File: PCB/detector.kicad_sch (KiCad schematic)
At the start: 17 parts, among them J6 Through, J8 Audio In, U2 TL072, U3 LM393

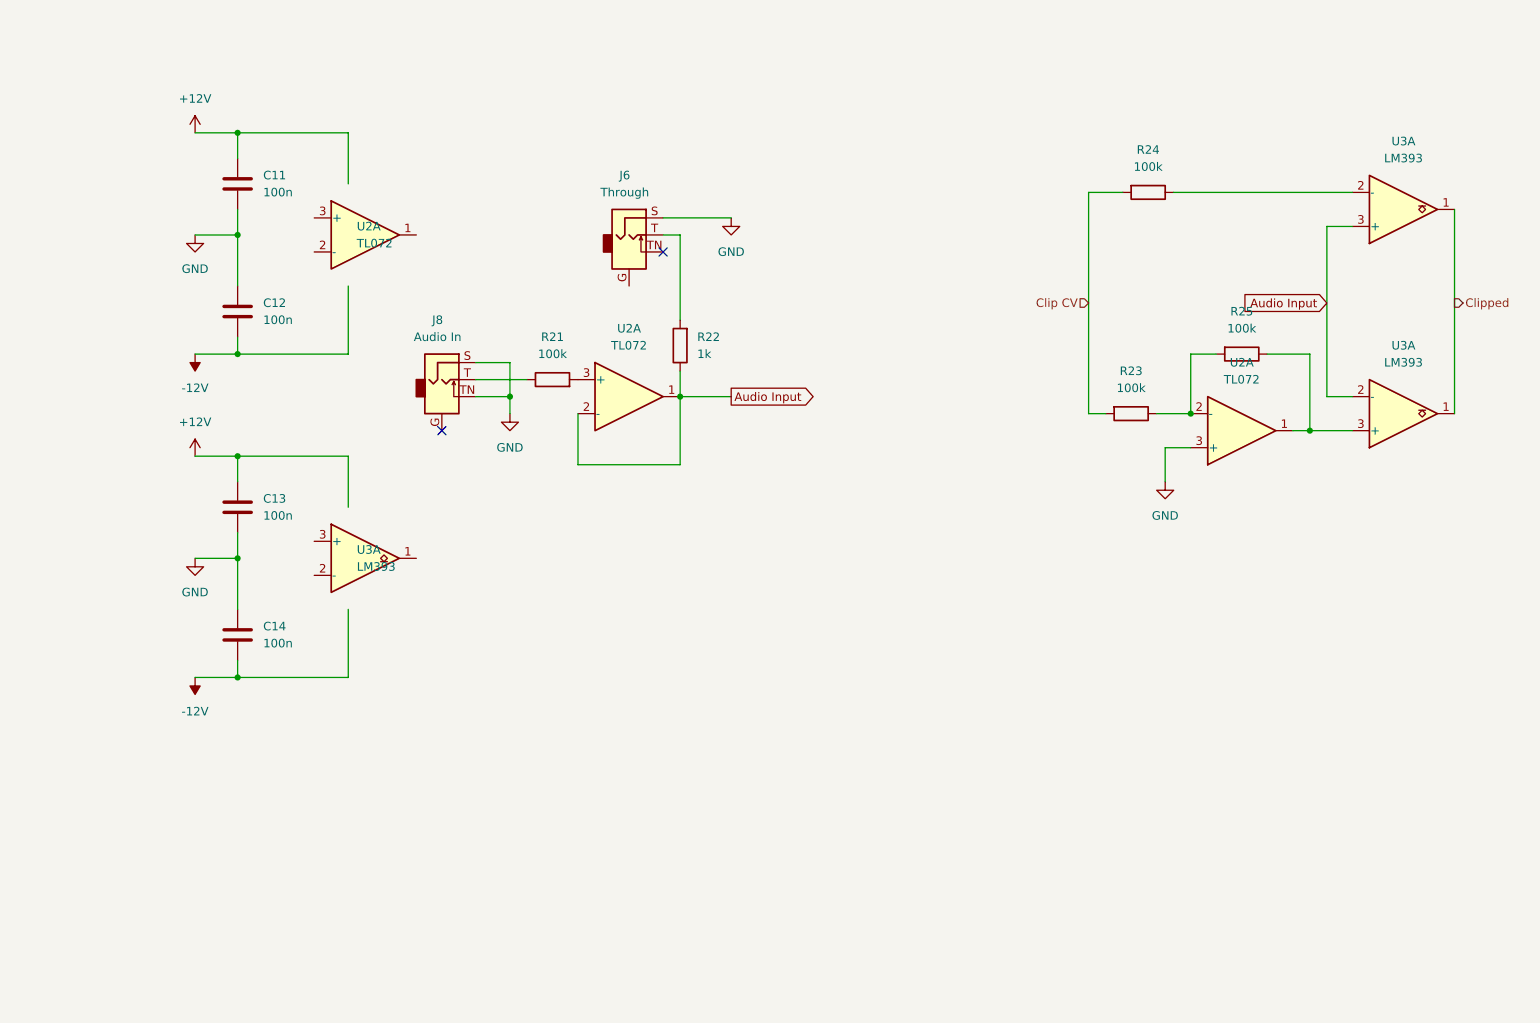
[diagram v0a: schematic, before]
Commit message: :art: Improve layout/positioning on main sheet
Also condense the voltage divider for the clip delay threshold,
as there is no load on this part and it can be shared between buffers.
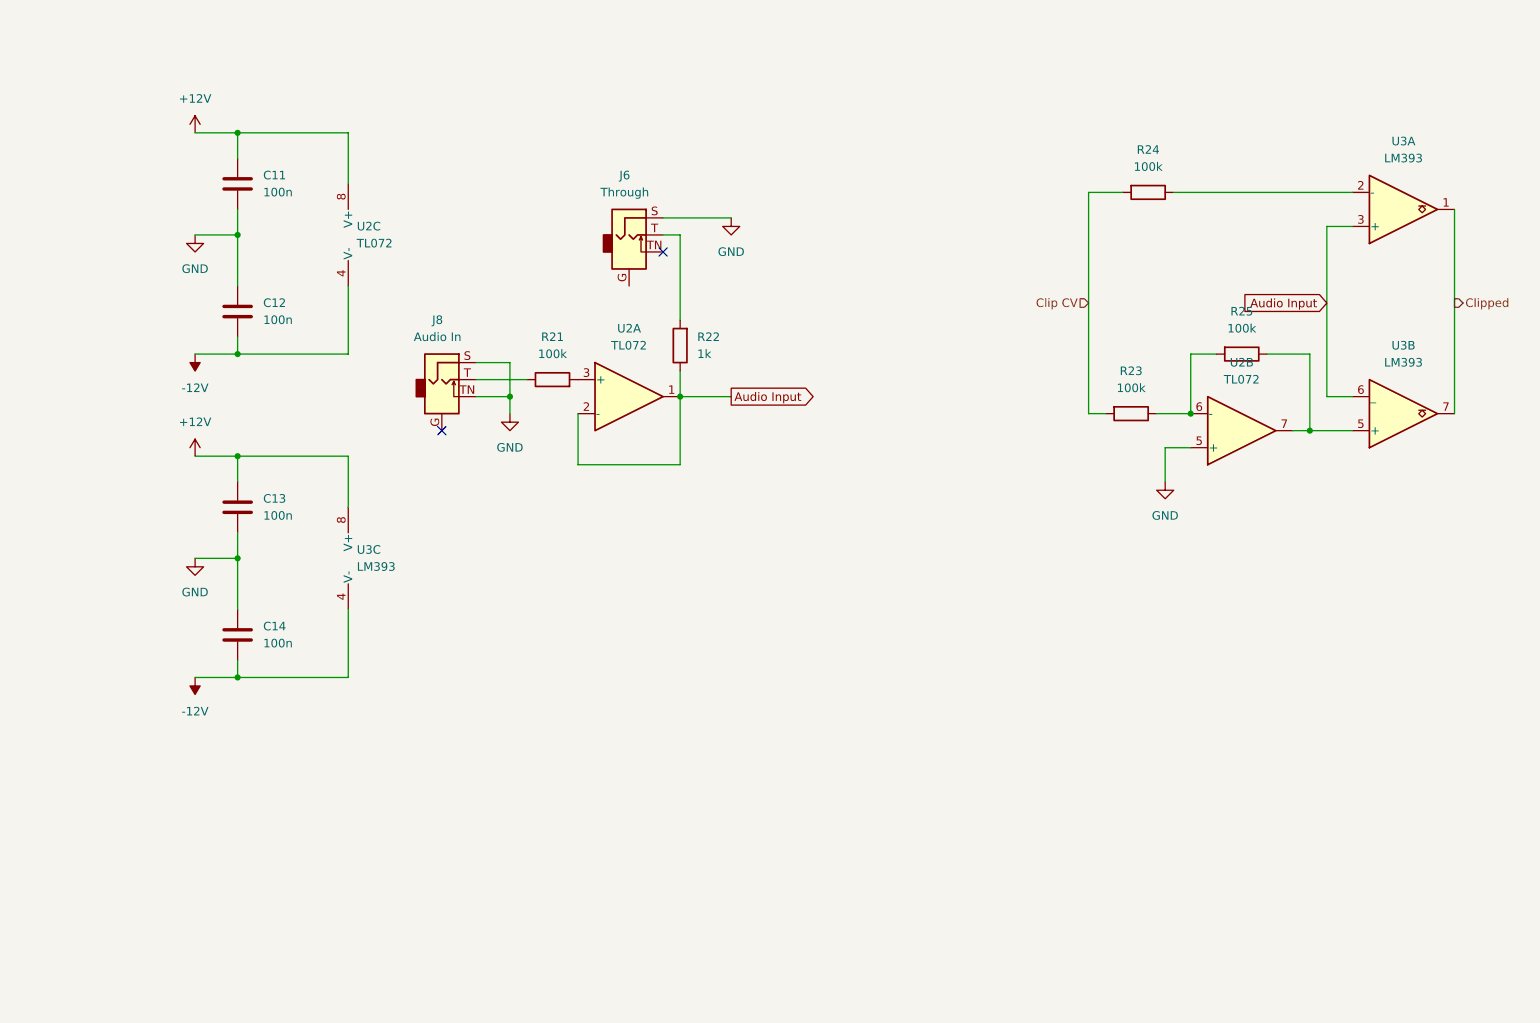
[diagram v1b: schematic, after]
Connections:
- net +12V: now also U2.8 (V+), U3.8 (V+)
- net -12V: now also U2.4 (V-), U3.4 (V-)
- net Audio Input: now also U3.6 (_); no longer U3.2 (-)
- net Clipped: now also U3.7; no longer U3.1
- net GND: now also U2.5 (+); no longer U2.3 (+)
- net at R23.1, R25.2: now also U2.6 (-); no longer U2.2 (-)
- new net: R25.1, U2.7, U3.5 (+)

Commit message: :bug: Rearrange detector and replace global label
Global labels in hierarchical sheets lead to connected traces, as the
label will be connected by name globally.

Replaced the global label in "Detector" by a wire.
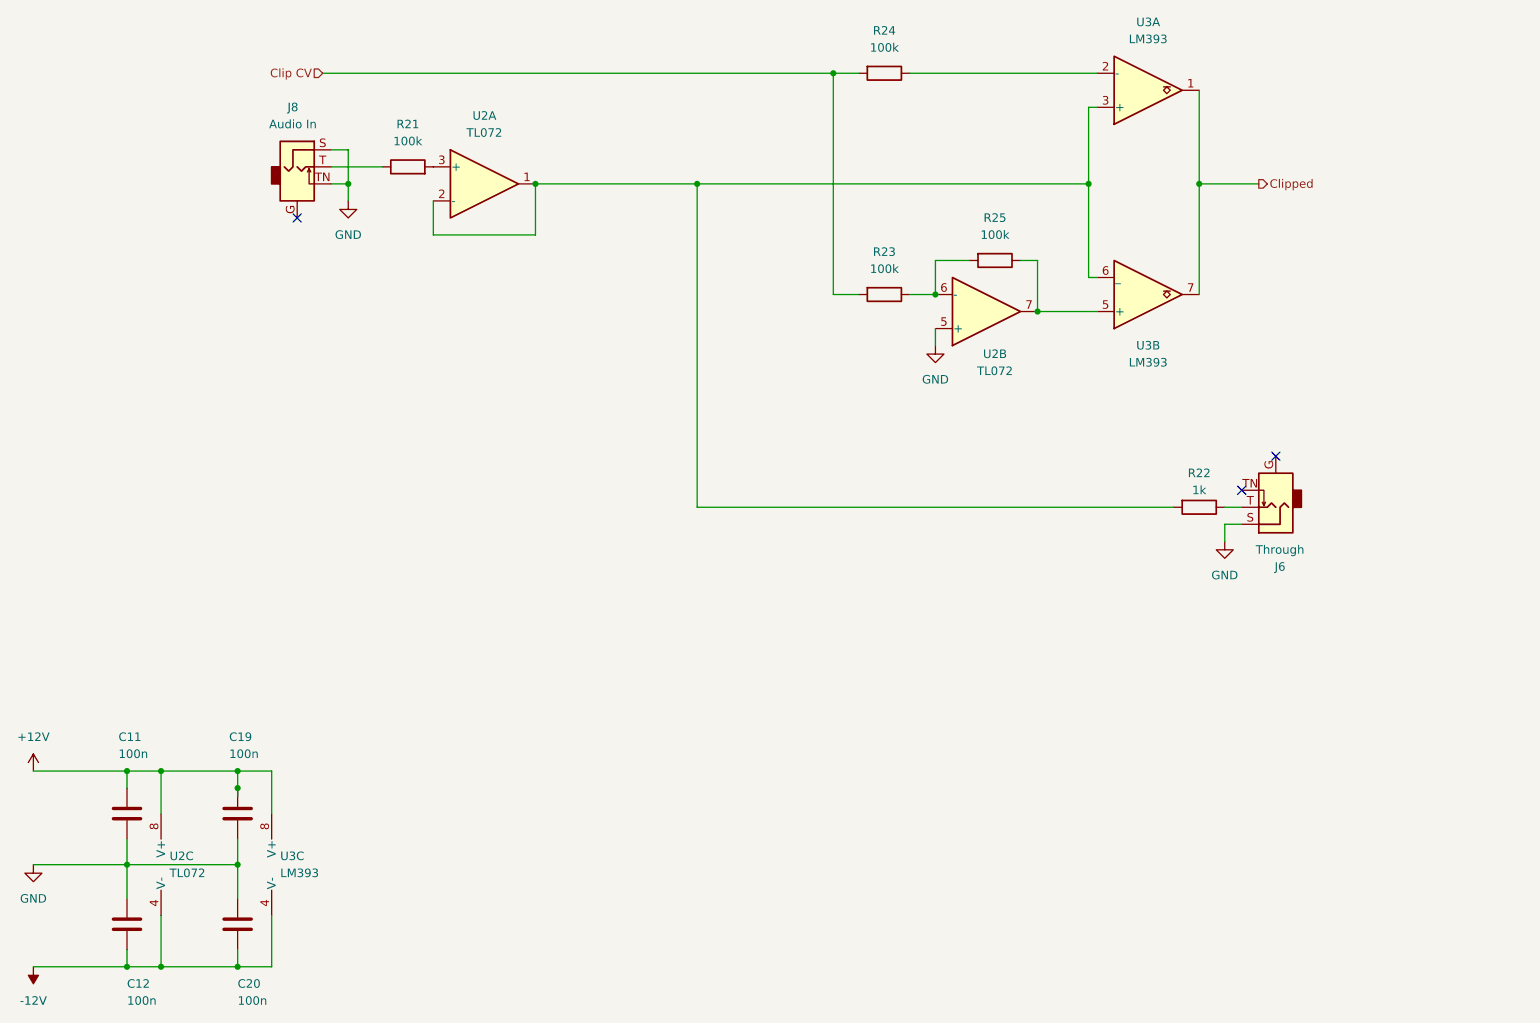
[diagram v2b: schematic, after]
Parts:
- removed C13, C14: 100n, Capacitor_THT:C_Disc_D4.3mm_W1.9mm_P5.00mm, symbol Device:C
- added C19, C20: 100n, Capacitor_THT:C_Disc_D4.3mm_W1.9mm_P5.00mm, symbol Device:C
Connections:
- net +12V: now also C19.1
- net -12V: now also C20.2
- net GND: now also C19.2, C20.1
- net at J6.T: now also R22.1; no longer R22.2
- net Audio Input: no longer names the net of U2.1, U2.2 (-), U3.3 (+), U3.6 (_)
- net Audio Input: now also R22.2; no longer R22.1
- no-connect marks 2 -> 3
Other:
- moved on the sheet: C11, C12, J6, J8, R21, R22, R23, R24, R25, U2A, U2B, U2C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

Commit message: :wrench: Re-assign component designators
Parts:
- renumbered C19 to C13, C20 to C14, J8 to J6, J6 to J7, R21 to R19, R24 to R20, R23 to R21, R25 to R22, R22 to R23

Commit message: :wrench: Replace audio jack footprints by centered versions
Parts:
- J6, J7: footprint Connector_Audio:Jack_3.5mm_QingPu_WQP-PJ398SM_Vertical_CircularHoles -> mopsy:Jack_3.5mm_QingPu_WQP-PJ398SM_Vertical_CircularHoles_Centered
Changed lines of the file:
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@@
       (effects (font (size 1.27 1.27)))
     )
-    (property "Footprint" "Connector_Audio:Jack_3.5mm_QingPu_WQP-PJ398SM_Vertical_CircularHoles" (at 209.55 116.84 0)
+    (property "Footprint" "mopsy:Jack_3.5mm_QingPu_WQP-PJ398SM_Vertical_CircularHoles_Centered" (at 209.55 116.84 0)
       (effects (font (size 1.27 1.27)) hide)
     )
@@
       (effects (font (size 1.27 1.27)))
     )
-    (property "Footprint" "Connector_Audio:Jack_3.5mm_QingPu_WQP-PJ398SM_Vertical_CircularHoles" (at 63.5 66.04 0)
+    (property "Footprint" "mopsy:Jack_3.5mm_QingPu_WQP-PJ398SM_Vertical_CircularHoles_Centered" (at 63.5 66.04 0)
       (effects (font (size 1.27 1.27)) hide)
     )

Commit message: PCB layout ready for production
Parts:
- R21: footprint Resistor_THT:R_Axial_DIN0207_L6.3mm_D2.5mm_P7.62mm_Horizontal -> R_Axial_DIN0207_L6.3mm_D2.5mm_P2.54mm_Vertical
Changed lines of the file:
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@@
   (symbol (lib_id "Device:R") (at 151.13 85.09 270) (unit 1)
     (in_bom yes) (on_board yes) (dnp no) (fields_autoplaced)
-    (property "Reference" "R21" (at 151.13 78.74 90)
+    (property "Reference" "R21" (at 151.13 80.01 90)
       (effects (font (size 1.27 1.27)))
     )
-    (property "Value" "100k" (at 151.13 81.28 90)
+    (property "Value" "100k" (at 151.13 82.55 90)
       (effects (font (size 1.27 1.27)))
     )
-    (property "Footprint" "Resistor_THT:R_Axial_DIN0207_L6.3mm_D2.5mm_P7.62mm_Horizontal" (at 151.13 83.312 90)
+    (property "Footprint" "R_Axial_DIN0207_L6.3mm_D2.5mm_P2.54mm_Vertical" (at 151.13 83.312 90)
       (effects (font (size 1.27 1.27)) hide)
     )

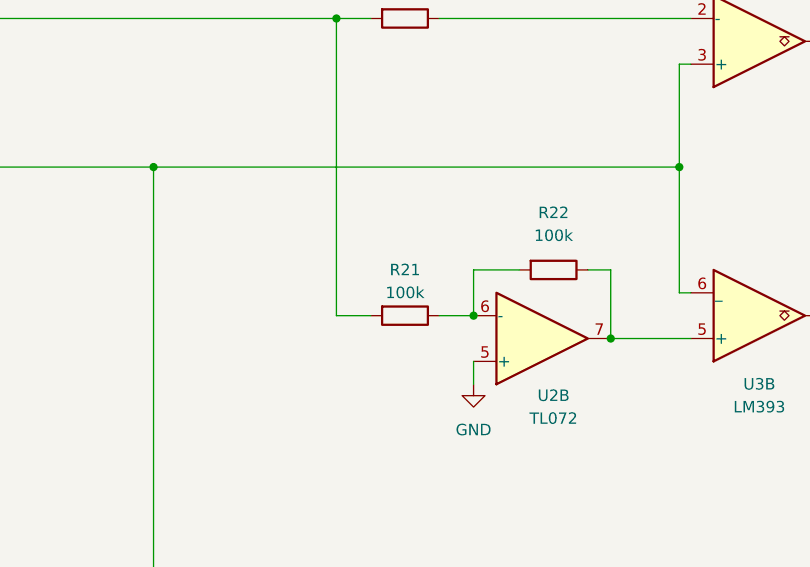
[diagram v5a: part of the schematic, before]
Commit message: :art: Try for a design where ICs do not cover jacks
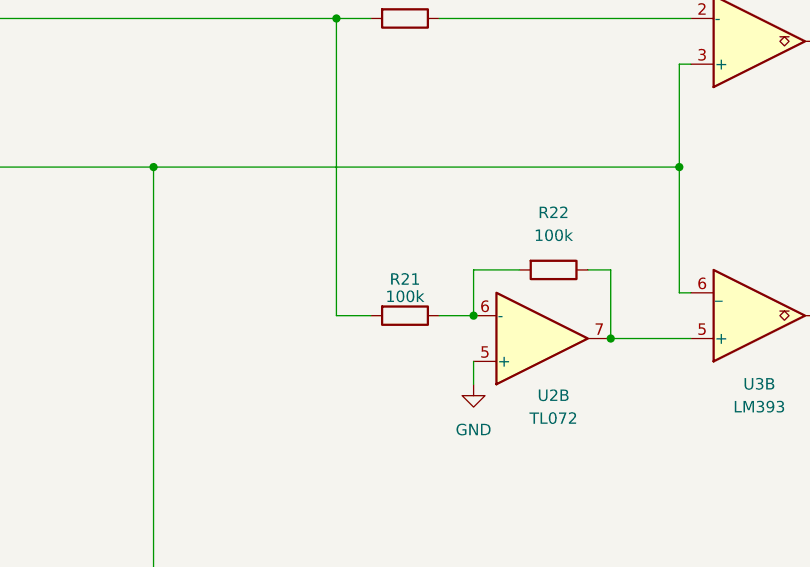
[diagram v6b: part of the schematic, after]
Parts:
- R21: footprint R_Axial_DIN0207_L6.3mm_D2.5mm_P2.54mm_Vertical -> Resistor_THT:R_Axial_DIN0207_L6.3mm_D2.5mm_P7.62mm_Horizontal
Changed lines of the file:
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@@
   (symbol (lib_id "Device:R") (at 151.13 85.09 270) (unit 1)
     (in_bom yes) (on_board yes) (dnp no) (fields_autoplaced)
-    (property "Reference" "R21" (at 151.13 80.01 90)
+    (property "Reference" "R21" (at 151.13 81.0641 90)
       (effects (font (size 1.27 1.27)))
     )
-    (property "Value" "100k" (at 151.13 82.55 90)
+    (property "Value" "100k" (at 151.13 82.9851 90)
       (effects (font (size 1.27 1.27)))
     )
-    (property "Footprint" "R_Axial_DIN0207_L6.3mm_D2.5mm_P2.54mm_Vertical" (at 151.13 83.312 90)
+    (property "Footprint" "Resistor_THT:R_Axial_DIN0207_L6.3mm_D2.5mm_P7.62mm_Horizontal" (at 151.13 83.312 90)
       (effects (font (size 1.27 1.27)) hide)
     )
